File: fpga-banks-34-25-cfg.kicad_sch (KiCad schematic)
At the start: 49 parts, among them J13 62000311121, Q12 2N7002_SOT-23-3, Q13 2N7002_SOT-23-3, Q14 2N7002_SOT-23-3, Q15 2N7002_SOT-23-3, Q16 2N7002_SOT-23-3, U14 XC7A100T-FGG484

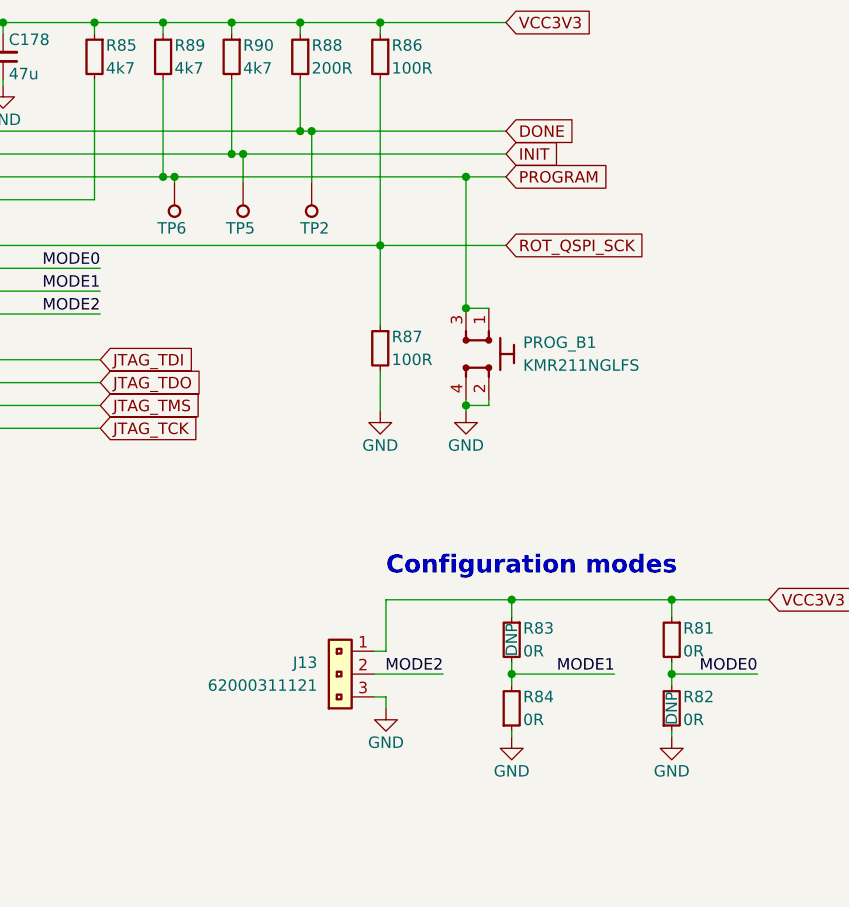
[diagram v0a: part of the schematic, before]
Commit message: [#55652] Fix hotareas
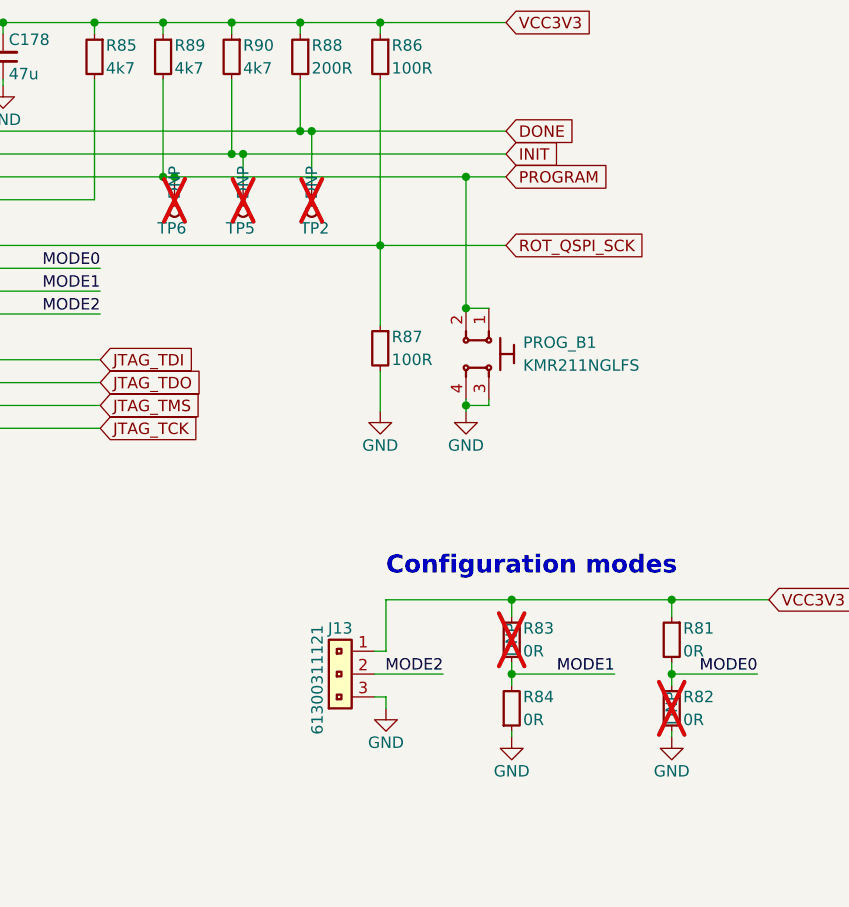
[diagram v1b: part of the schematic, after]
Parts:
- D10, D11, D12, D13, D9: Manufacturer Osram -> OSRAM
- J13: value 62000311121 -> PinHeader_1x3_P2.54mm_Drill1.1mm; footprint antmicro-footprints:PinHeader_1x3_P2.54_Drill1.1mm -> antmicro-footprints:PinHeader_1x3_P2.54mm_Drill1.1mm; symbol antmicroRectangularConnectorsHeadersMalePins:PinHeader_1x3_P2.54mm_Drill1.1mm -> antmicroGenericPinHeaders:PinHeader_1x3_P2.54mm_Drill1.1mm; VSD_class (none) -> IO Header
- PROG_B1: value SW_SPST_KMR211NGLFS -> SW_KMR211NGLFS_SMD; footprint antmicro-footprints:SW_SPST_4.2x2.8 -> antmicro-footprints:SW_KMR211NGLFS_SMD; symbol antmicroPushbuttonSwitches:SW_SPST_KMR211NGLFS -> antmicroPushbuttonSwitches:SW_KMR211NGLFS_SMD
- R82, R83: now not fitted; now left out of the parts list
- TP2, TP5, TP6: value TP_SMD1MM -> TP_1mm_SMD; footprint antmicro-footprints:Testpoint_smd_1mm -> antmicro-footprints:TP_SMD_1mm; now not fitted; now left out of the parts list
- U14: footprint antmicro-footprints:BGA-484_23x23mm_Layout22x22_P1mm_Xilinx_FGG484 -> antmicro-footprints:BGA-484_23x23mm_Layout22x22_P1mm_FGG484; symbol antmicroMicrocontrollers:XC7A100T-FGG484 -> antmicroFPGAChips:XC7A100T-FGG484; Manufacturer Xilinx -> AMD-Xilinx
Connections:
- net GND: now also PROG_B1.3; no longer PROG_B1.2
- net PROGRAM: now also PROG_B1.2; no longer PROG_B1.3

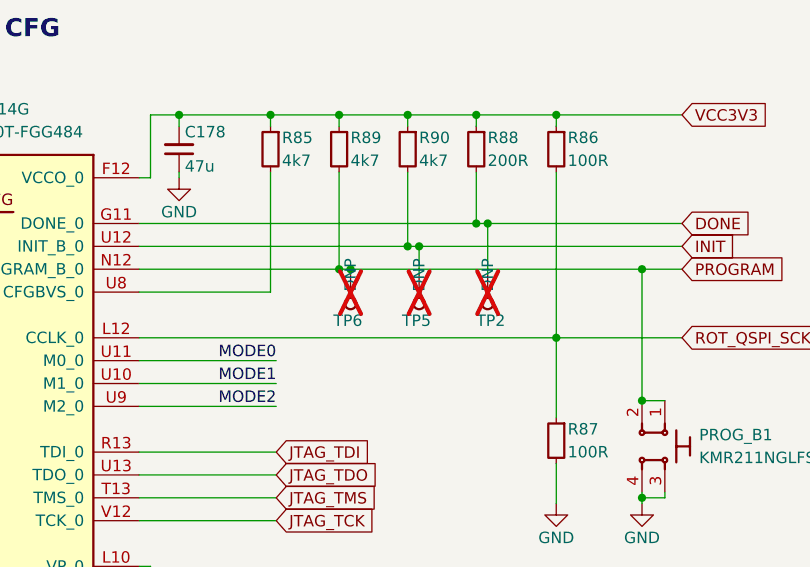
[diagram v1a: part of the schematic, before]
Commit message: [#68236] Update components description
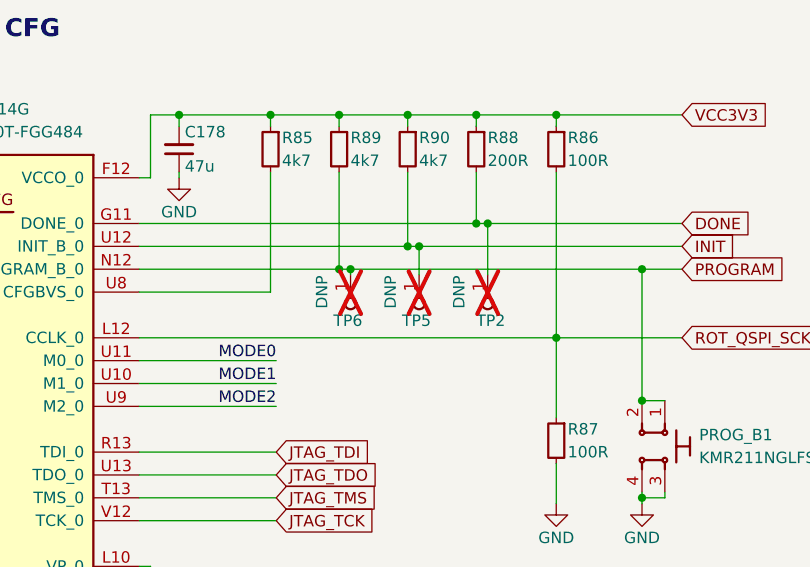
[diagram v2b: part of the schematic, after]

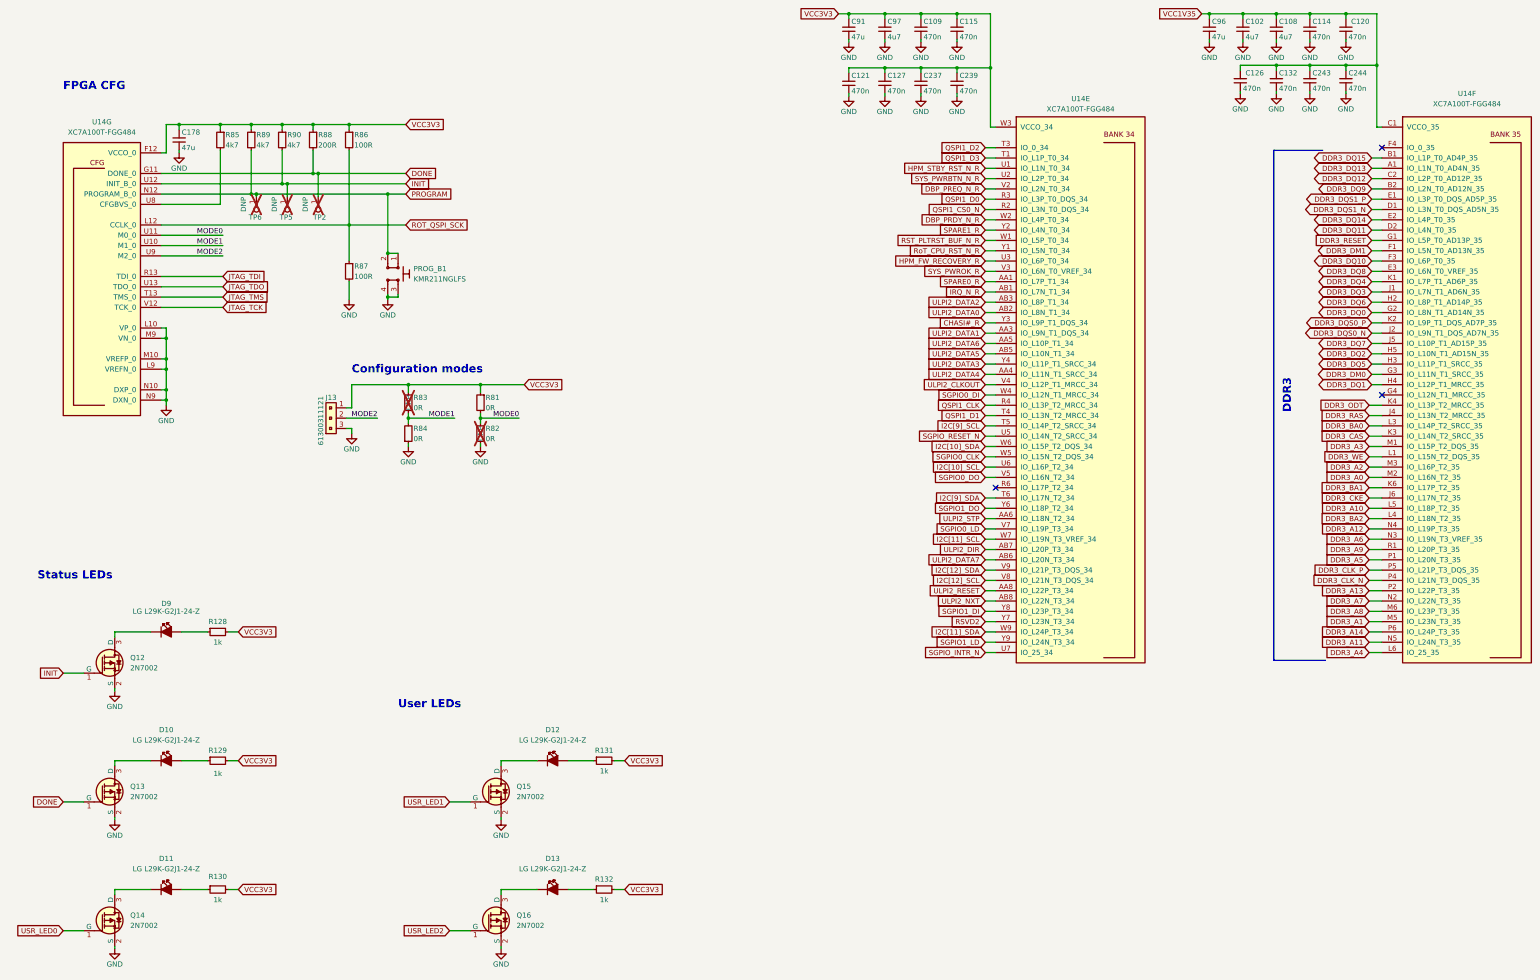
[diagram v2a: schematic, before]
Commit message: [#68236] Allign sch to grid
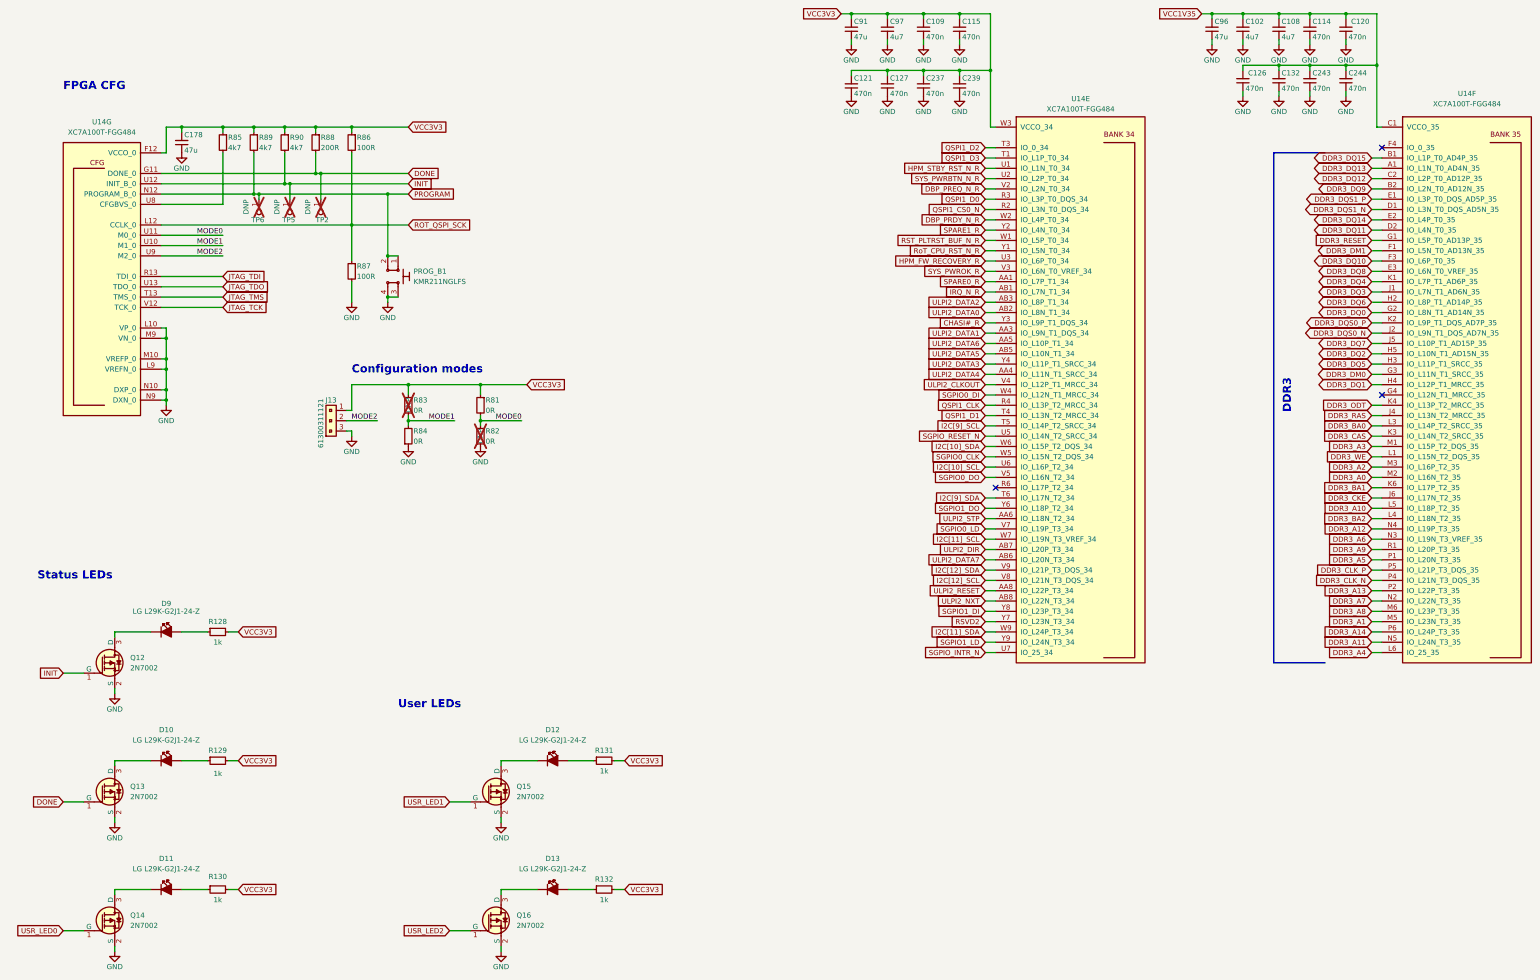
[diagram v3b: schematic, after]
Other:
- moved on the sheet: C108, C109, C115, C121, C126, C127, C132, C178, C237, C239, C91, C96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

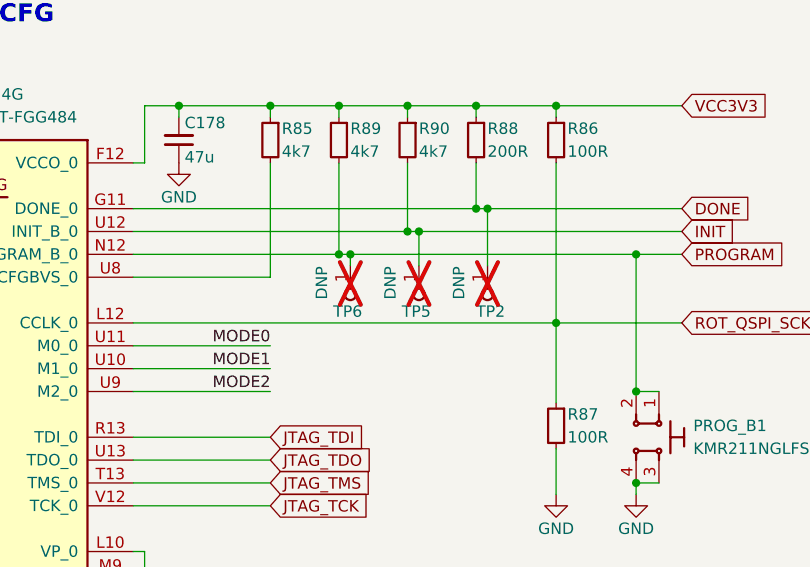
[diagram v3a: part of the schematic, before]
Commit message: [#68236] Remove DNP property from Testpoints
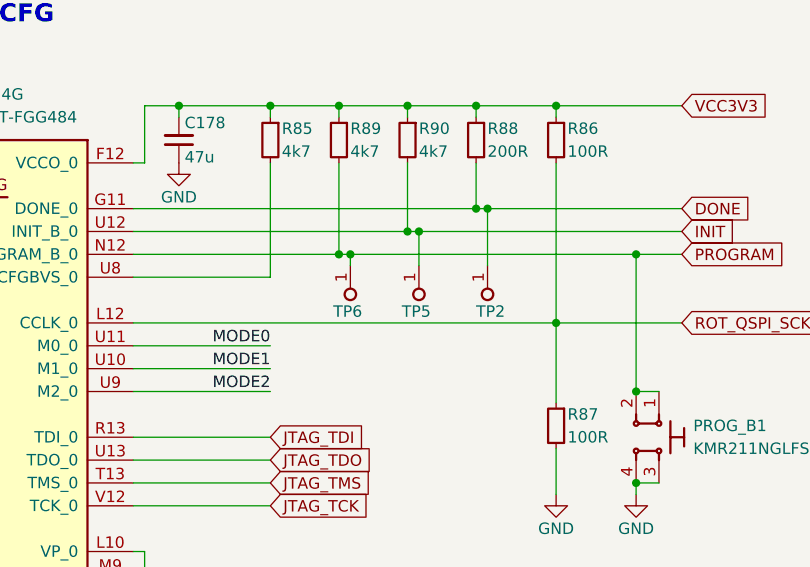
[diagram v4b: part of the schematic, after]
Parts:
- TP2, TP5, TP6: DNP DNP -> (none); now fitted
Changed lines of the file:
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@@
   )
   (symbol (lib_id "antmicroTestPoints:TP_1mm_SMD") (at 101.6 90.17 270) (unit 1)
-    (in_bom no) (on_board yes) (dnp yes)
+    (in_bom no) (on_board yes) (dnp no)
     (property "Reference" "TP2" (at 100.33 95.25 90)
       (effects (font (size 1.27 1.27)) (justify left))
@@
       (effects (font (size 1.27 1.27) (thickness 0.15)) (justify left bottom) hide)
     )
-    (property "DNP" "DNP" (at 98.425 92.075 0)
-      (effects (font (size 1.27 1.27)))
-    )
     (pin "1")
     (instances
@@
   )
   (symbol (lib_id "antmicroTestPoints:TP_1mm_SMD") (at 86.36 90.17 270) (unit 1)
-    (in_bom no) (on_board yes) (dnp yes)
+    (in_bom no) (on_board yes) (dnp no)
     (property "Reference" "TP6" (at 84.455 95.25 90)
       (effects (font (size 1.27 1.27)) (justify left))
@@
     (property "License" "Apache-2.0" (at 68.58 105.41 0)
       (effects (font (size 1.27 1.27) (thickness 0.15)) (justify left bottom) hide)
-    )
-    (property "DNP" "DNP" (at 83.185 92.075 0)
-      (effects (font (size 1.27 1.27)))
     )
     (pin "1")
@@
   )
   (symbol (lib_id "antmicroTestPoints:TP_1mm_SMD") (at 93.98 90.17 270) (unit 1)
-    (in_bom no) (on_board yes) (dnp yes)
+    (in_bom no) (on_board yes) (dnp no)
     (property "Reference" "TP5" (at 92.075 95.25 90)
       (effects (font (size 1.27 1.27)) (justify left))
@@
       (effects (font (size 1.27 1.27) (thickness 0.15)) (justify left bottom) hide)
     )
-    (property "DNP" "DNP" (at 90.805 92.075 0)
-      (effects (font (size 1.27 1.27)))
-    )
-    (pin "1")
+    (pin "1")
